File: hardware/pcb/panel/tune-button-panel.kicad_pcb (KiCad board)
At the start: 2 copper layers, 148 x 86.7 mm, 262 parts, among them J1 USB-C, J1 XIAO left, J2 LiPo, J2 XIAO right, J3 Buttons, J3 LiPo, J4 to XIAO BAT, Q1 AO3401A, SW1 MX switch, SW2 MX switch, SW3 MX switch, SW4 MX switch, SW5 RESET, SW6 BOOT, U1 ESP32-C3-WROOM-02-N4, U2 SRV05-4, U3 TP4054, U4 RT9080-3.3, U5 SRV05-4

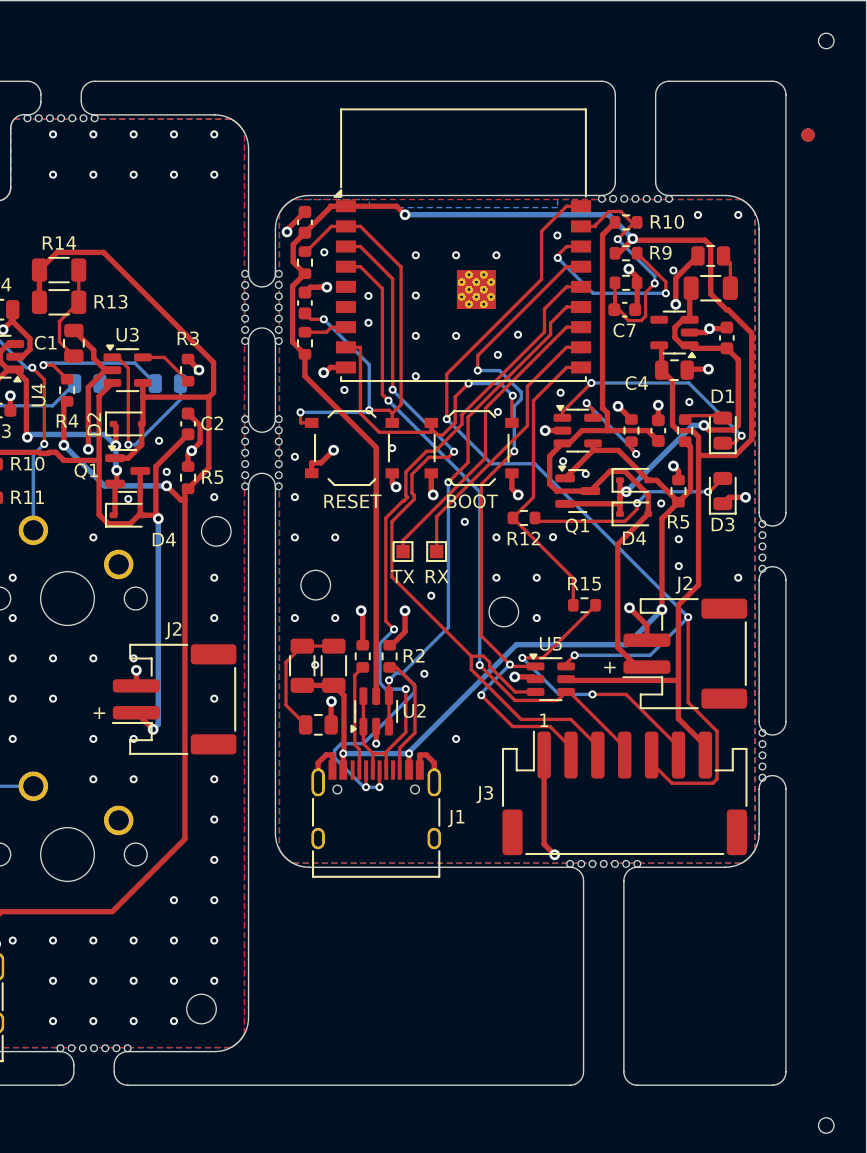
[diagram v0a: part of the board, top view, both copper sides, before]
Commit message: pcb: panel round-10 audit fixes: no tab within 1.5 mm of a pad (JLC mouse-bite rule), asserted
The reroute let c3-jst's top tab slide next to the module's corner pad (0.81 mm from a bite).
free_spans now holds every pad 1.5 mm from the bite line and panel.py exits if a tab ends up
closer. c3-jst gets five tabs; README tab text and pour-fragment comment updated.
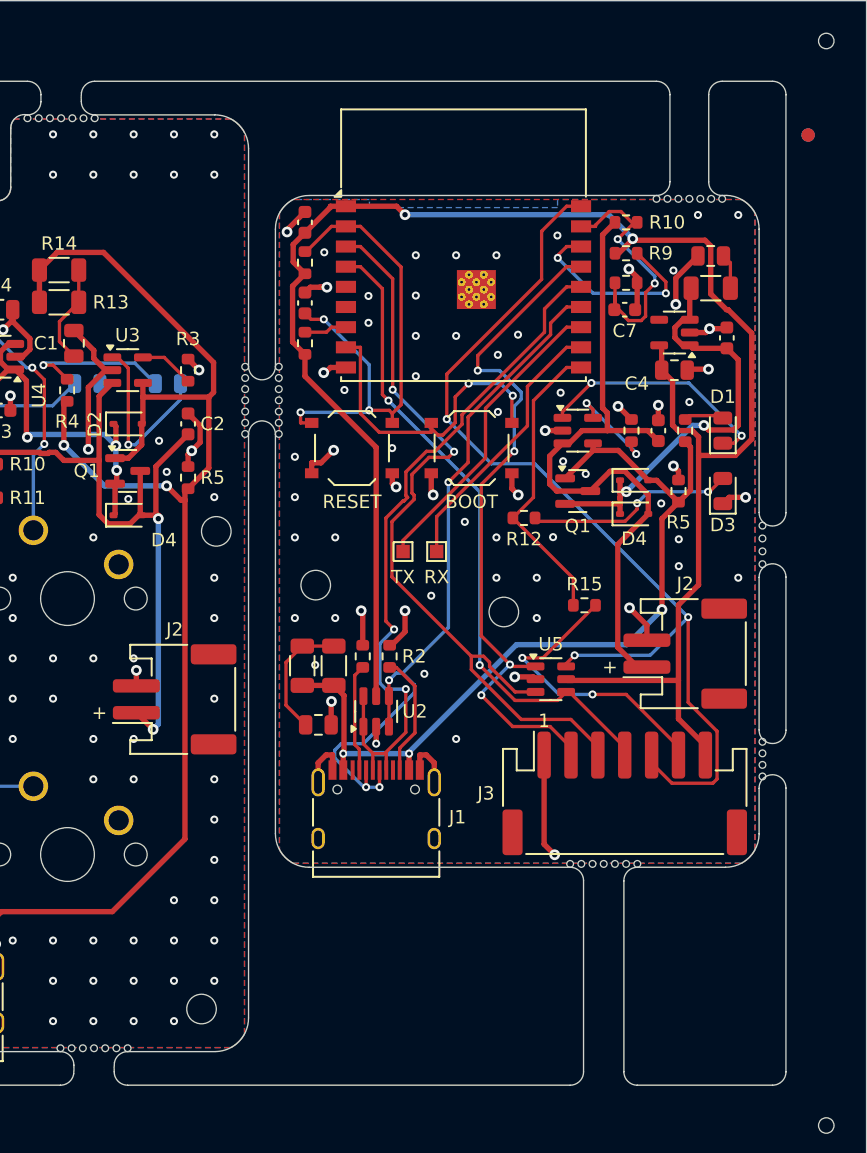
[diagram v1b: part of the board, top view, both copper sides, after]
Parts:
- removed KiKit_MB_19_1, KiKit_MB_19_6, KiKit_MB_19_7, KiKit_MB_20_1, KiKit_MB_20_6, KiKit_MB_20_7, KiKit_MB_21_2, KiKit_MB_21_3, KiKit_MB_21_4, KiKit_MB_21_5, KiKit_MB_21_6, KiKit_MB_22_2, KiKit_MB_22_3, KiKit_MB_22_4, KiKit_MB_22_5, KiKit_MB_22_6: NPTH, NPTH
- moved KiKit_MB_14_7 73.8 mm to (65.0, 70.5)
- moved KiKit_MB_14_6 73.2 mm to (65.8, 70.5)
- moved KiKit_MB_14_5 72.7 mm to (66.7, 70.5)
- moved KiKit_MB_14_4 72.2 mm to (67.5, 70.5)
- moved KiKit_MB_14_3 71.7 mm to (68.3, 70.5)
- moved KiKit_MB_14_2 71.3 mm to (69.2, 70.5)
- moved KiKit_MB_14_1 70.9 mm to (70.0, 70.5)
- moved KiKit_MB_16_7 53.3 mm to (104.2, 19.7)
- moved KiKit_MB_16_6 52.2 mm to (104.2, 20.6)
- moved KiKit_MB_16_5 51.2 mm to (104.2, 21.4)
- moved KiKit_MB_16_4 50.1 mm to (104.2, 22.2)
- moved KiKit_MB_16_3 49.1 mm to (104.2, 23.1)
- moved KiKit_MB_16_2 48.1 mm to (104.2, 23.9)
- moved KiKit_MB_16_1 47.1 mm to (104.2, 24.7)
- moved KiKit_MB_18_7 39.6 mm to (125.9, 56.8)
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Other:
- outline, holes or cut-outs redrawn

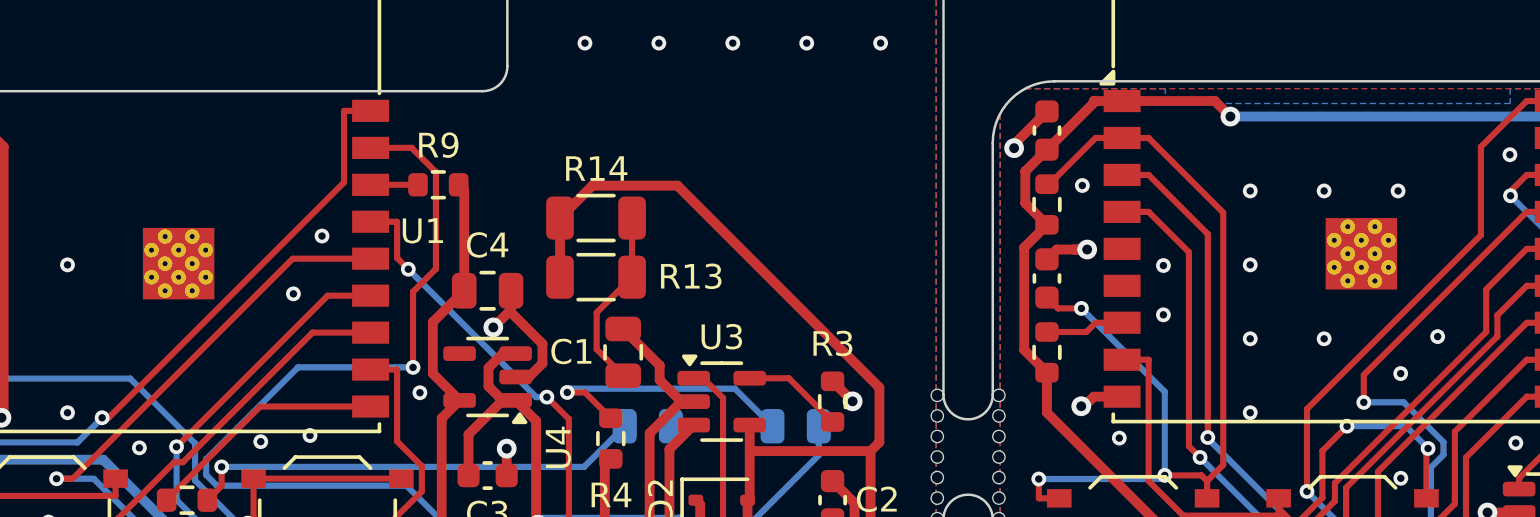
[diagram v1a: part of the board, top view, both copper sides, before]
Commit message: pcb: no hole under 0.3 mm (JLC standard): the module's 12 thermal vias go 0.2 -> 0.3 mm, DRC minimum 0.3
JLC prices 0.2 mm holes as an option: $20 -> $70 for the panel. Only those pad drills change;
copper, nets and positions are identical on all three boards.
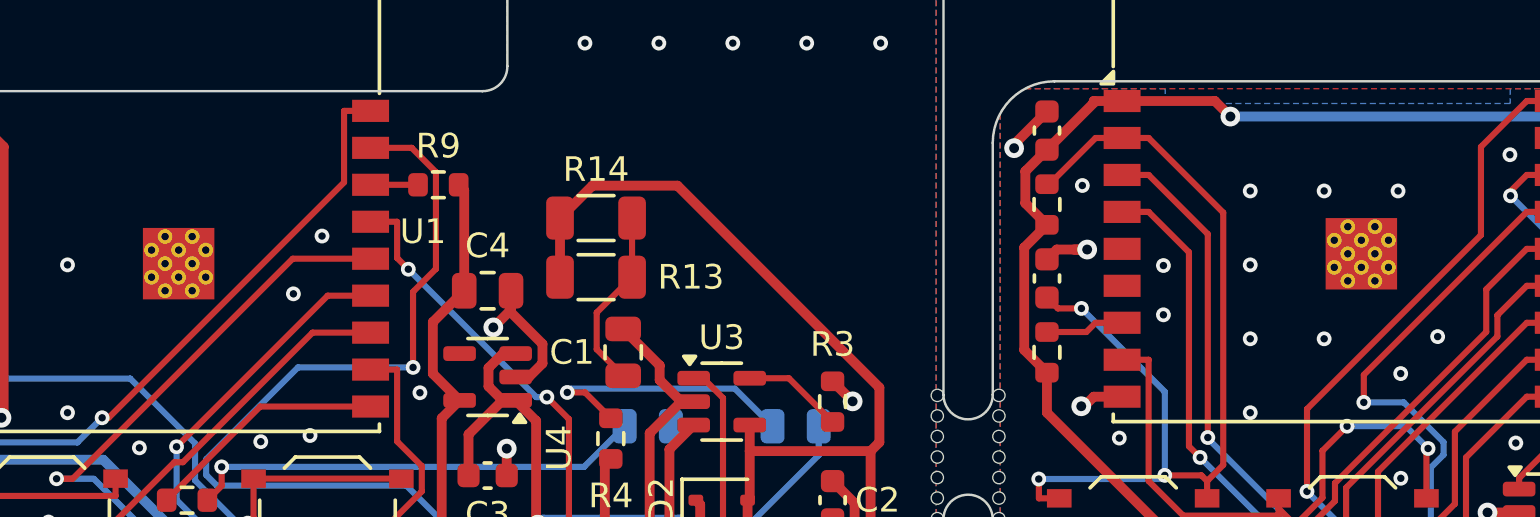
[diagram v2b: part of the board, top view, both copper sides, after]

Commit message: pcb: no JLCJLCJLCJLC order-number marker on any board (ordered with Remove Mark)
Only the marker text and its no-via rule area go; parts, copper and fills are identical, and the
BOM and CPL are unchanged. README says to choose Remove Mark.
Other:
- board text removed: "JLCJLCJLCJLC"
